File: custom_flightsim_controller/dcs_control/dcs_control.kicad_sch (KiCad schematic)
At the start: 9 parts, among them SW1 RotaryEncoder_Switch, SW2 RotaryEncoder_Switch, SW3 RotaryEncoder_Switch, SW4 SW_SPDT_MSM, SW5 SW_SPDT_MSM, SW6 SW_SPDT_MSM, SW7 SW_SPDT_MSM, SW8 SW_Push, U1 Sparkfun_Pro_Micro

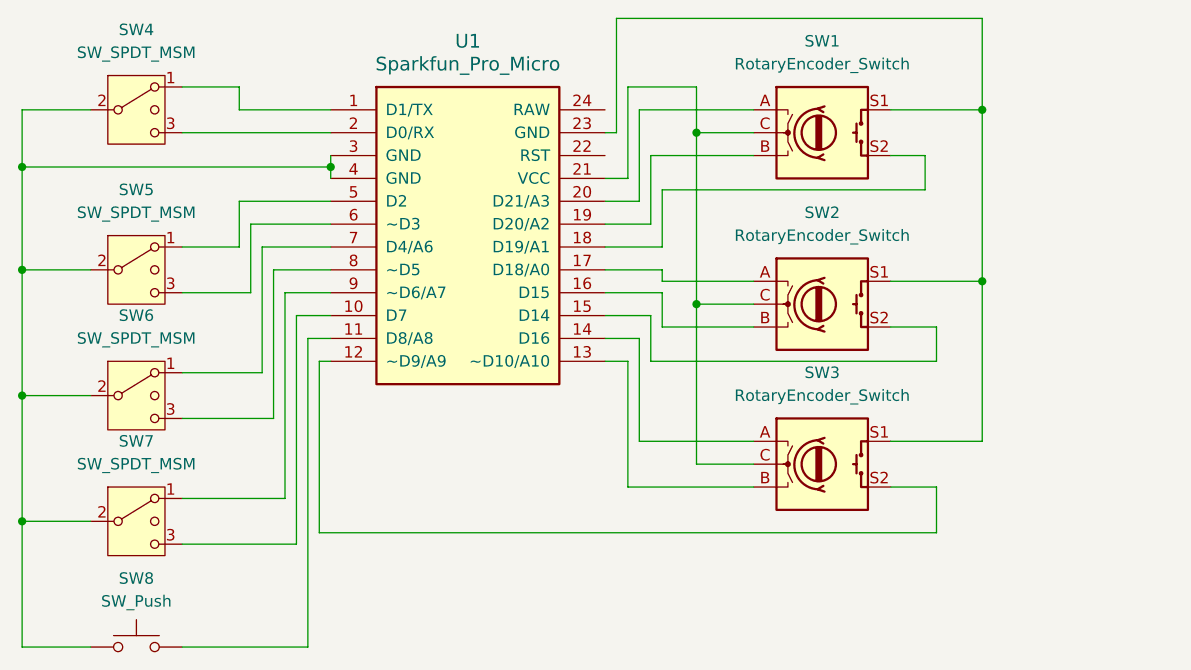
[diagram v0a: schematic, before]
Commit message: DcsControl: Updated schematics and exported all symbols to a library
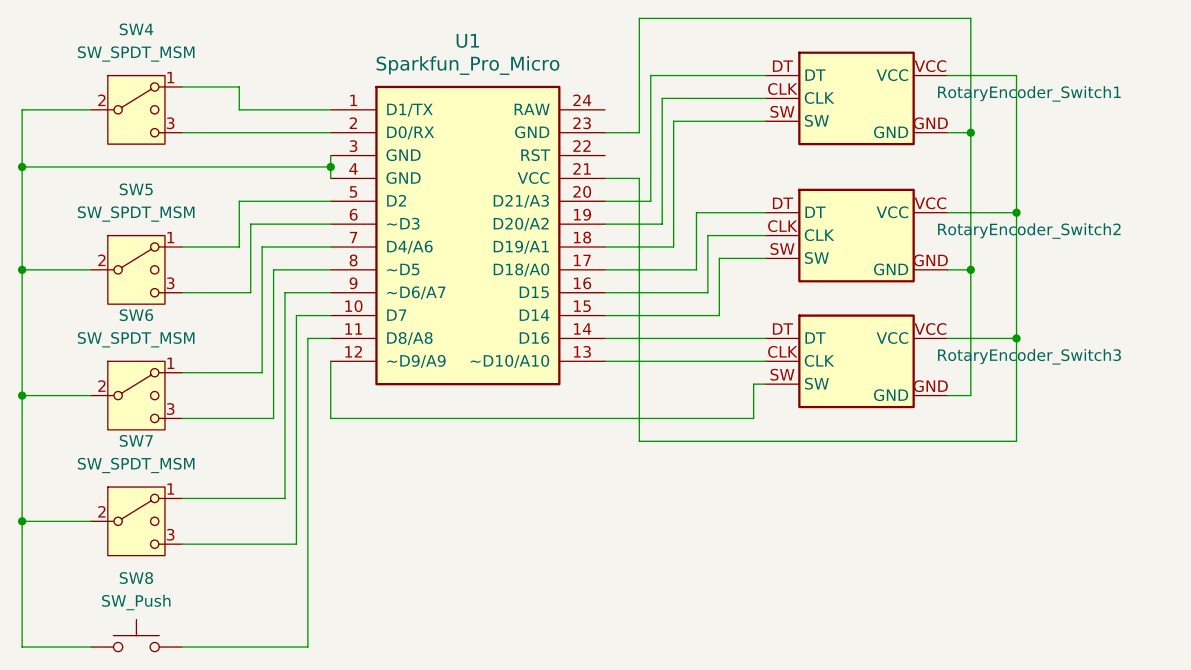
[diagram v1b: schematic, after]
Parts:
- removed SW1, SW2, SW3: RotaryEncoder_Switch, symbol Device:RotaryEncoder_Switch
- added RotaryEncoder_Switch1, RotaryEncoder_Switch2, RotaryEncoder_Switch3: ~, symbol ControllerSymbols:RotaryEncoder_Switch_KY40
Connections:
- net at U1.12 (~D9/A9): now also RotaryEncoder_Switch3.SW
- net at U1.13 (~D10/A10): now also RotaryEncoder_Switch3.CLK
- net at U1.14 (D16): now also RotaryEncoder_Switch3.DT
- net at U1.15 (D14): now also RotaryEncoder_Switch2.SW
- net at U1.16 (D15): now also RotaryEncoder_Switch2.CLK
- net at U1.17 (D18/A0): now also RotaryEncoder_Switch2.DT
- net at U1.18 (D19/A1): now also RotaryEncoder_Switch1.SW
- net at U1.19 (D20/A2): now also RotaryEncoder_Switch1.CLK
- net at U1.20 (D21/A3): now also RotaryEncoder_Switch1.DT
- net at U1.21 (VCC): now also RotaryEncoder_Switch1.VCC, RotaryEncoder_Switch2.VCC, RotaryEncoder_Switch3.VCC
- net at U1.23 (GND): now also RotaryEncoder_Switch1.GND, RotaryEncoder_Switch2.GND, RotaryEncoder_Switch3.GND
